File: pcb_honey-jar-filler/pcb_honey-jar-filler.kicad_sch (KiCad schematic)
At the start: 97 parts, among them J1 12V, J10 GPIO19, J11 GPIO23, J12 MOS2 out (FWD, Drain), J13 230V Heater, J14 5V, J15 5V, J16 GPIO15, J17 GND, J18 GND, J19 Servo, J2 12V, J20 Conn_01x07_Pin, J22 Reserve, J23 LED1, J24 load-cell (red, black), J25 load-cell (white, green), J26 B+ B- (free), J27 Supply, J28 Relay fallback, J29 LED2, J3 3V3, J30 OLED, J31 rotary-encoder, J4 reserve Buttons, J5 4...7V, J6 Pos-switch, J7 Load-cell (HX711 input), J8 MOS1 out (FWD, Drain), K4 RT314A24, K6 Relay_LEG-12, K7 Relay_LEG-12, M2 DC-worm-gear motor (Carousell), Q1 IRLB8721PBF, Q2 IRLB8721PBF, Q6 IRF5305, U1 esp32-devkit-v1_30Pin, U10 LM2576T-ADJ, U3 ULN2003, U4 HX711_24-bit-ADC_weight-scale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, U9 LM2576T-5

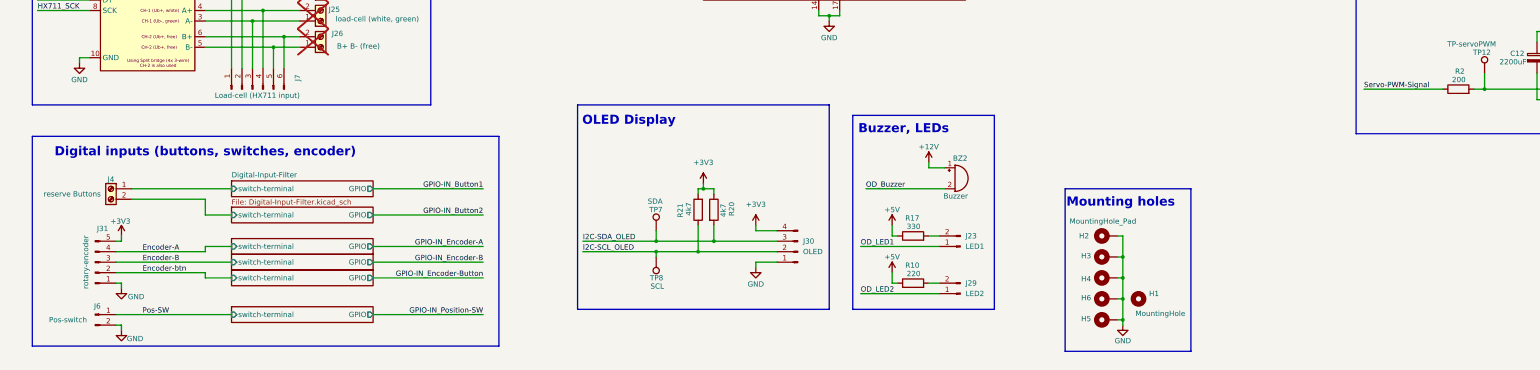
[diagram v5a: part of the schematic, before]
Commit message: pcb: Update actually soldered filter R values (use sub-sheet parameters)
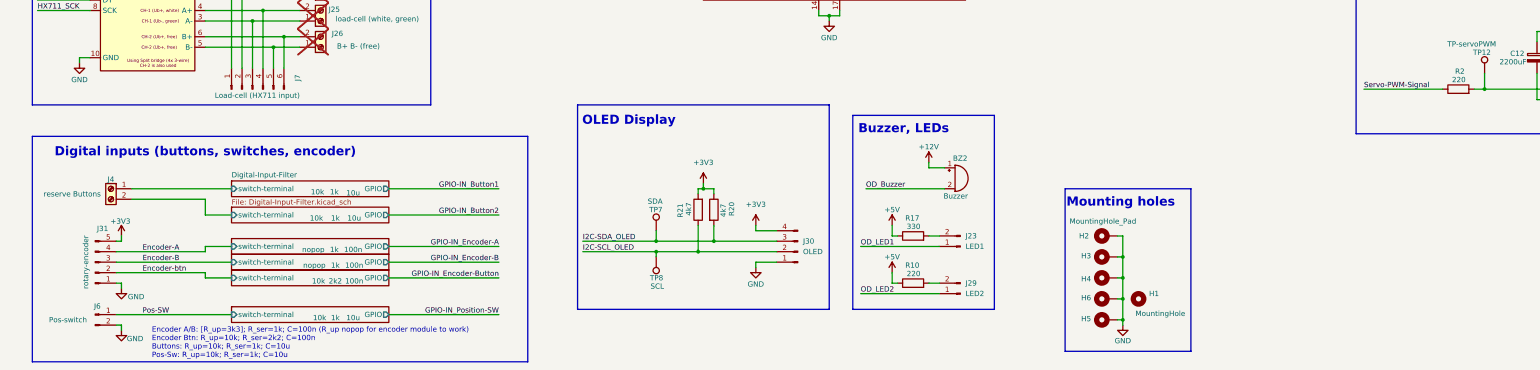
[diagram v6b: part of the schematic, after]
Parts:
- R2: value 200 -> 220
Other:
- note added: "Encoder A/B: [R_up=3k3]; R_ser=1k; C=100n (R_up nopop for encoder module to work) Encoder Btn: R_up=10k; R_ser=2k2; C=100n Buttons: R_up=10k; R_ser=1k; C=10u Pos-Sw: R_up=10k; R_ser=1k; C=10u"
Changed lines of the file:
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@@
 	(rectangle
 		(start 16.51 229.87)
-		(end 129.54 280.67)
+		(end 136.525 284.48)
 		(stroke
 			(width 0)
@@
 		)
 	)
+	(text "Encoder A/B: [R_up=3k3]; R_ser=1k; C=100n (R_up nopop for encoder module to work)\nEncoder Btn: R_up=10k; R_ser=2k2; C=100n\nButtons: R_up=10k; R_ser=1k; C=10u\nPos-Sw: R_up=10k; R_ser=1k; C=10u"
+		(exclude_from_sim no)
+		(at 45.466 276.098 0)
+		(effects
+			(font
+				(size 1.27 1.27)
+			)
+			(justify left top)
+		)
+	)
 	(text "Buzzer, LEDs"
 		(exclude_from_sim no)
@@
 	(wire
 		(pts
-			(xy 125.73 256.54) (xy 99.06 256.54)
+			(xy 129.54 256.54) (xy 102.87 256.54)
 		)
 		(stroke
@@
 	(wire
 		(pts
-			(xy 125.73 242.57) (xy 99.06 242.57)
+			(xy 129.54 242.57) (xy 102.87 242.57)
 		)
 		(stroke
@@
 	(wire
 		(pts
-			(xy 125.73 273.05) (xy 99.06 273.05)
+			(xy 129.54 273.05) (xy 102.87 273.05)
 		)
 		(stroke
@@
 	(wire
 		(pts
-			(xy 125.73 260.35) (xy 99.06 260.35)
+			(xy 129.54 260.35) (xy 102.87 260.35)
 		)
 		(stroke
@@
 	(wire
 		(pts
-			(xy 125.73 264.16) (xy 99.06 264.16)
+			(xy 129.54 264.16) (xy 102.87 264.16)
 		)
 		(stroke
@@
 	(wire
 		(pts
-			(xy 99.06 248.92) (xy 125.73 248.92)
+			(xy 102.87 248.92) (xy 129.54 248.92)
 		)
 		(stroke
@@
 	)
 	(label "GPIO-IN_Encoder-Button"
-		(at 125.73 264.16 180)
+		(at 129.54 264.16 180)
 		(effects
 			(font
@@
 	)
 	(label "GPIO-IN_Position-SW"
-		(at 125.73 273.05 180)
+		(at 129.54 273.05 180)
 		(effects
 			(font
@@
 	)
 	(label "GPIO-IN_Button1"
-		(at 125.73 242.57 180)
+		(at 129.54 242.57 180)
 		(effects
 			(font
@@
 	)
 	(label "GPIO-IN_Encoder-B"
-		(at 125.73 260.35 180)
+		(at 129.54 260.35 180)
 		(effects
 			(font
@@
 	)
 	(label "GPIO-IN_Encoder-A"
-		(at 125.73 256.54 180)
+		(at 129.54 256.54 180)
 		(effects
 			(font
@@
 	)
 	(label "GPIO-IN_Button2"
-		(at 125.73 248.92 180)
+		(at 129.54 248.92 180)
 		(effects
 			(font
@@
 			)
 		)
-		(property "Value" "200"
+		(property "Value" "220"
 			(at 363.728 216.154 90)
 			(effects
@@
 	(sheet
 		(at 64.77 240.665)
-		(size 34.29 3.81)
+		(size 38.1 3.81)
 		(exclude_from_sim no)
 		(in_bom yes)
 		(on_board yes)
 		(dnp no)
-		(fields_autoplaced yes)
 		(stroke
 			(width 0.1524)
@@
 			)
 		)
+		(property "R_pullup" "10k"
+			(at 85.598 243.332 0)
+			(effects
+				(font
+					(size 1.27 1.27)
+				)
+			)
+		)
+		(property "R_series" "1k"
+			(at 89.662 243.332 0)
+			(effects
+				(font
+					(size 1.27 1.27)
+				)
+			)
+		)
+		(property "C_filter" "10u"
+			(at 94.234 243.586 0)
+			(effects
+				(font
+					(size 1.27 1.27)
+				)
+			)
+		)
 		(pin "GPIO" output
-			(at 99.06 242.57 0)
+			(at 102.87 242.57 0)
 			(effects
 				(font
@@
 	(sheet
 		(at 64.77 262.255)
-		(size 34.29 3.81)
+		(size 38.1 3.81)
 		(exclude_from_sim no)
 		(in_bom yes)
 		(on_board yes)
 		(dnp no)
-		(fields_autoplaced yes)
 		(stroke
 			(width 0.1524)
@@
 			)
 		)
+		(property "R_pullup" "10k"
+			(at 85.852 264.922 0)
+			(effects
+				(font
+					(size 1.27 1.27)
+				)
+			)
+		)
+		(property "R_series" "2k2"
+			(at 89.916 264.922 0)
+			(effects
+				(font
+					(size 1.27 1.27)
+				)
+			)
+		)
+		(property "C_filter" "100n"
+			(at 94.488 264.922 0)
+			(effects
+				(font
+					(size 1.27 1.27)
+				)
+			)
+		)
 		(pin "GPIO" output
-			(at 99.06 264.16 0)
+			(at 102.87 264.16 0)
 			(effects
 				(font
@@
 	(sheet
 		(at 64.77 247.015)
-		(size 34.29 3.81)
+		(size 38.1 3.81)
 		(exclude_from_sim no)
 		(in_bom yes)
 		(on_board yes)
 		(dnp no)
-		(fields_autoplaced yes)
 		(stroke
 			(width 0.1524)
@@
 			)
 		)
+		(property "R_pullup" "10k"
+			(at 85.344 249.682 0)
+			(effects
+				(font
+					(size 1.27 1.27)
+				)
+			)
+		)
+		(property "R_series" "1k"
+			(at 89.916 249.682 0)
+			(effects
+				(font
+					(size 1.27 1.27)
+				)
+			)
+		)
+		(property "C_filter" "10u"
+			(at 94.488 249.682 0)
+			(effects
+				(font
+					(size 1.27 1.27)
+				)
+			)
+		)
 		(pin "GPIO" output
-			(at 99.06 248.92 0)
+			(at 102.87 248.92 0)
 			(effects
 				(font
@@
 	(sheet
 		(at 64.77 254.635)
-		(size 34.29 3.81)
+		(size 38.1 3.81)
 		(exclude_from_sim no)
 		(in_bom yes)
 		(on_board yes)
 		(dnp no)
-		(fields_autoplaced yes)
 		(stroke
 			(width 0.1524)
@@
 			)
 		)
+		(property "R_pullup" "nopop"
+			(at 84.582 257.302 0)
+			(effects
+				(font
+					(size 1.27 1.27)
+				)
+			)
+		)
+		(property "R_series" "1k"
+			(at 89.662 257.302 0)
+			(effects
+				(font
+					(size 1.27 1.27)
+				)
+			)
+		)
+		(property "C_filter" "100n"
+			(at 94.234 257.302 0)
+			(effects
+				(font
+					(size 1.27 1.27)
+				)
+			)
+		)
 		(pin "GPIO" output
-			(at 99.06 256.54 0)
+			(at 102.87 256.54 0)
 			(effects
 				(font
@@
 	(sheet
 		(at 64.77 271.145)
-		(size 34.29 3.81)
+		(size 38.1 3.81)
 		(exclude_from_sim no)
 		(in_bom yes)
 		(on_board yes)
 		(dnp no)
-		(fields_autoplaced yes)
 		(stroke
 			(width 0.1524)
@@
 			)
 		)
+		(property "R_pullup" "10k"
+			(at 86.106 273.812 0)
+			(effects
+				(font
+					(size 1.27 1.27)
+				)
+			)
+		)
+		(property "R_series" "1k"
+			(at 89.916 273.812 0)
+			(effects
+				(font
+					(size 1.27 1.27)
+				)
+			)
+		)
+		(property "C_filter" "10u"
+			(at 94.234 273.812 0)
+			(effects
+				(font
+					(size 1.27 1.27)
+				)
+			)
+		)
 		(pin "GPIO" output
-			(at 99.06 273.05 0)
+			(at 102.87 273.05 0)
 			(effects
 				(font
@@
 	(sheet
 		(at 64.77 258.445)
-		(size 34.29 3.81)
+		(size 38.1 3.81)
 		(exclude_from_sim no)
 		(in_bom yes)
 		(on_board yes)
 		(dnp no)
-		(fields_autoplaced yes)
 		(stroke
 			(width 0.1524)
@@
 			)
 		)
+		(property "R_pullup" "nopop"
+			(at 84.836 261.112 0)
+			(effects
+				(font
+					(size 1.27 1.27)
+				)
+			)
+		)
+		(property "R_series" "1k"
+			(at 89.916 261.112 0)
+			(effects
+				(font
+					(size 1.27 1.27)
+				)
+			)
+		)
+		(property "C_filter" "100n"
+			(at 94.488 261.112 0)
+			(effects
+				(font
+					(size 1.27 1.27)
+				)
+			)
+		)
 		(pin "GPIO" output
-			(at 99.06 260.35 0)
+			(at 102.87 260.35 0)
 			(effects
 				(font

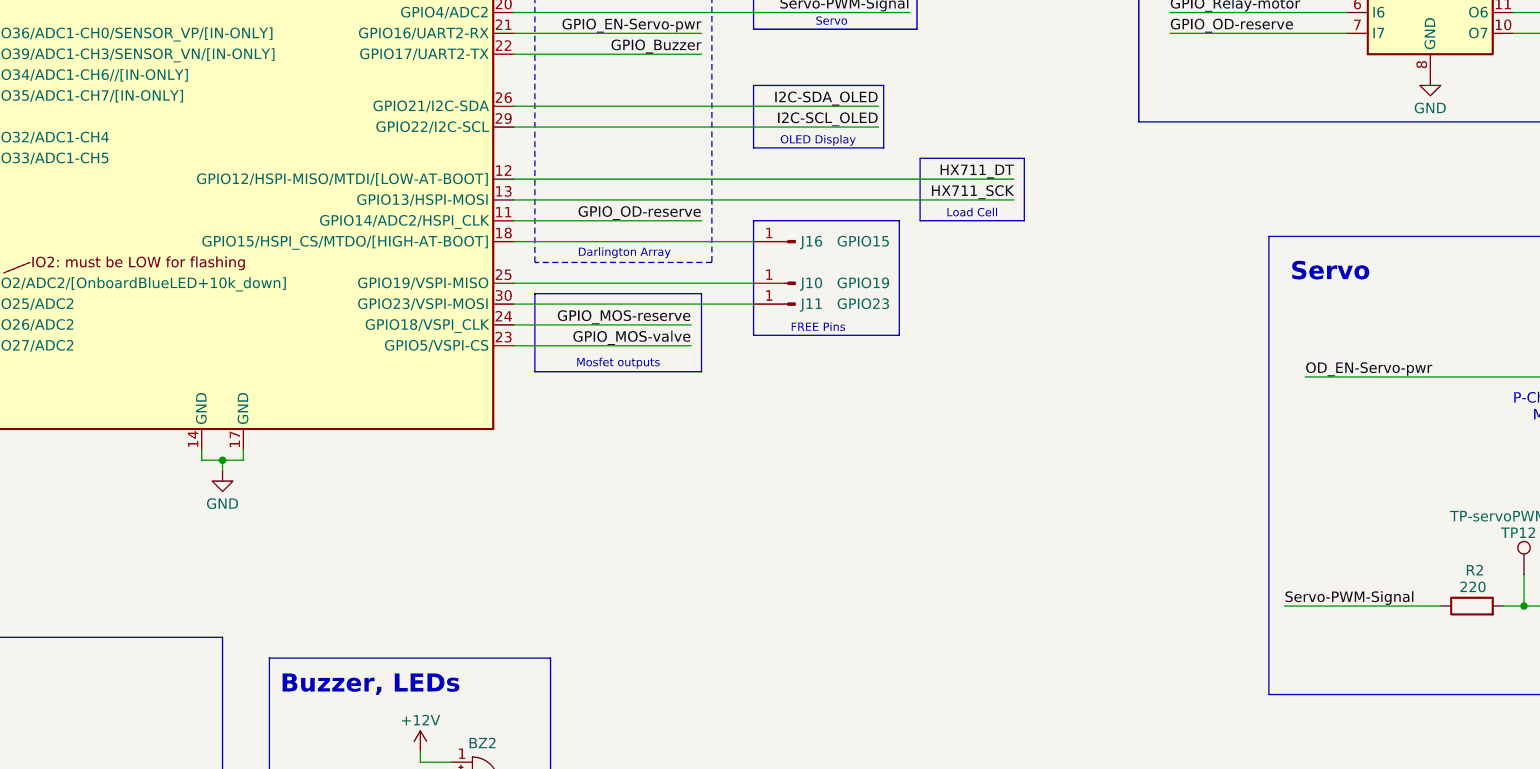
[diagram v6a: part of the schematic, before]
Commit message: Fix crash on nvs-write: Change H711 DT-pin (non strapping), Add notes to schematic + pcb
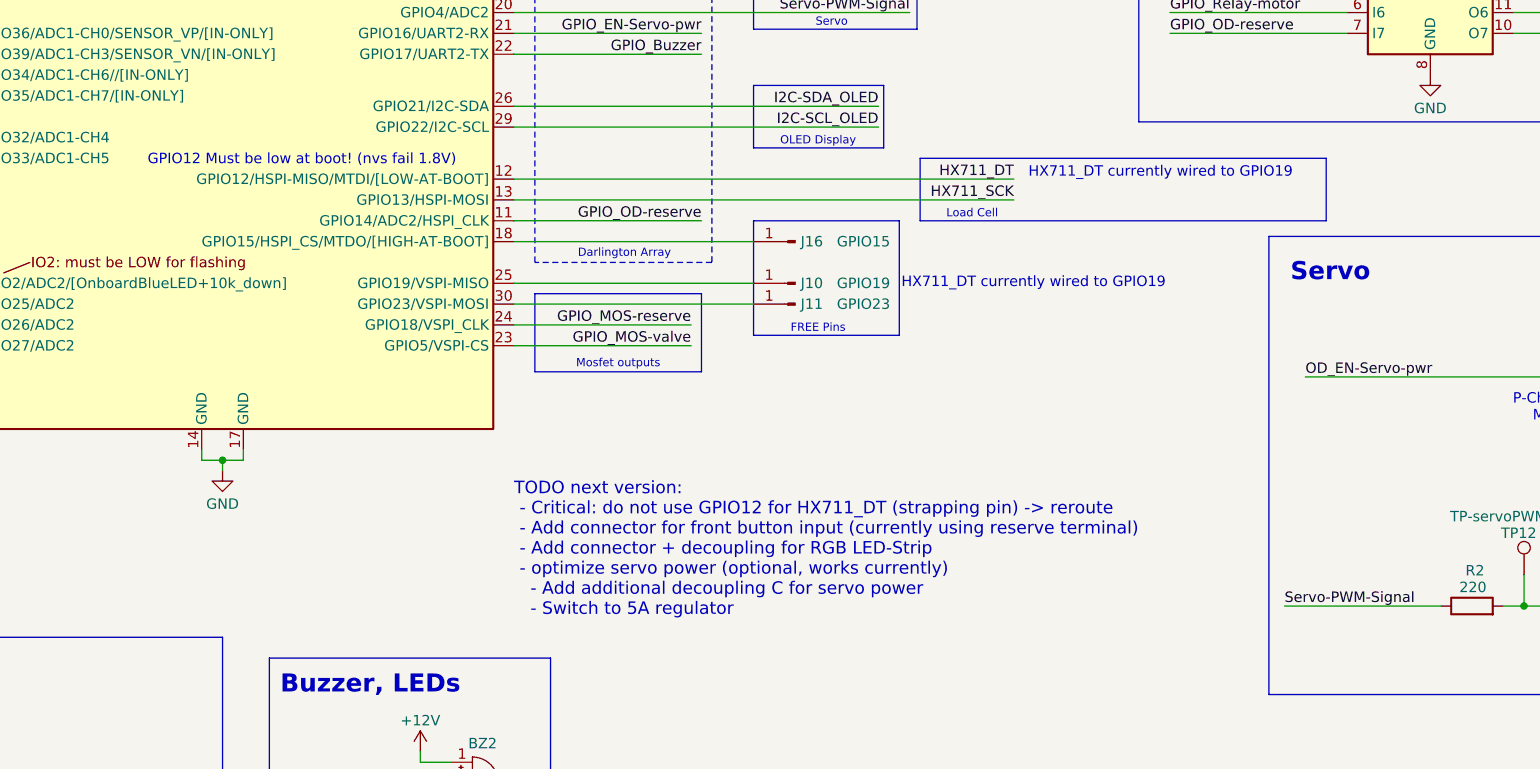
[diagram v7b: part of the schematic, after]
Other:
- note added: "GPIO12 Must be low at boot! (nvs fail 1.8V)"
- note added: "HX711_DT currently wired to GPIO19"
- note added: "TODO next version: - Critical: do not use GPIO12 for HX711_DT (strapping pin) -> reroute - Add connector for front button input (currently using reserve terminal) - Add connector + decoupling for RGB LED-Strip - optimize servo power (optional, works currently) - Add additional decoupling C for servo power - Switch to 5A regulator"
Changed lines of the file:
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@@
 	(rectangle
 		(start 294.64 163.83)
-		(end 307.34 171.45)
+		(end 344.17 171.45)
 		(stroke
 			(width 0)
@@
 		)
 	)
+	(text "GPIO12 Must be low at boot! (nvs fail 1.8V)"
+		(exclude_from_sim no)
+		(at 200.406 164.084 0)
+		(effects
+			(font
+				(size 1.27 1.27)
+			)
+			(justify left)
+		)
+	)
 	(text "Power terminals, testpoints"
 		(exclude_from_sim no)
@@
 		)
 	)
+	(text "TODO next version:\n - Critical: do not use GPIO12 for HX711_DT (strapping pin) -> reroute\n - Add connector for front button input (currently using reserve terminal)\n - Add connector + decoupling for RGB LED-Strip\n - optimize servo power (optional, works currently)\n   - Add additional decoupling C for servo power\n   - Switch to 5A regulator"
+		(exclude_from_sim no)
+		(at 245.11 211.582 0)
+		(effects
+			(font
+				(size 1.524 1.524)
+			)
+			(justify left)
+		)
+	)
 	(text "Encoder A/B: [R_up=3k3]; R_ser=1k; C=100n (R_up nopop for encoder module to work)\nEncoder Btn: R_up=10k; R_ser=2k2; C=100n\nButtons: R_up=10k; R_ser=1k; C=10u\nPos-Sw: R_up=10k; R_ser=1k; C=10u"
 		(exclude_from_sim no)
@@
 		)
 	)
+	(text "HX711_DT currently wired to GPIO19"
+		(exclude_from_sim no)
+		(at 307.848 165.608 0)
+		(effects
+			(font
+				(size 1.27 1.27)
+			)
+			(justify left)
+		)
+	)
 	(text "1: used for USB\n3: used for USB"
 		(exclude_from_sim no)
@@
 		)
 	)
+	(text "HX711_DT currently wired to GPIO19"
+		(exclude_from_sim no)
+		(at 292.354 179.07 0)
+		(effects
+			(font
+				(size 1.27 1.27)
+			)
+			(justify left)
+		)
+	)
